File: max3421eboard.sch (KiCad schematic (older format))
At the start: 26 parts, among them J1 USB A, J2 USB MicroB, J3 1x10, J4 1x8, J5 1x8, J6 1x3, J7 Conn_01x04, U1 MAX3421E, U2 LP2985-3.3, U3 STMPS2141STR, Y1 12MHz

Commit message: Added more filtering/bypass and revised layout
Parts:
- added C8: 1u, Capacitors_SMD:C_0805_HandSoldering, symbol Device:C
- added C9: 100n, Capacitors_SMD:C_0805_HandSoldering, symbol Device:C
- added L1: 120 @ 100MHz, Inductors_SMD:L_0805_HandSoldering, symbol Device:L_Core_Ferrite
- U1: symbol MAX3421E:MAX3421E -> max3421eboard-rescue:MAX3421E-MAX3421E
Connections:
- net +3V3: now also C9.1
- net GND: now also C8.2, C9.2
- net VBUS: now also C8.1; no longer J1.1 (VBUS), J7.1 (Pin_1)
- net at C6.1, U1.22 (VBCOMP), U3.1 (OUT): now also J6.3 (Pin_3), J7.1 (Pin_1), L1.1; no longer J2.1 (VBUS), J6.1 (Pin_1)
- net at U3.5 (IN): now also J6.1 (Pin_1); no longer J6.3 (Pin_3)
- new net: J1.1 (VBUS), J2.1 (VBUS), L1.2
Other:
- moved on the sheet: C1, C2, C3, C4, C6, C7, J1, J2, J3, J4, J5, J6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

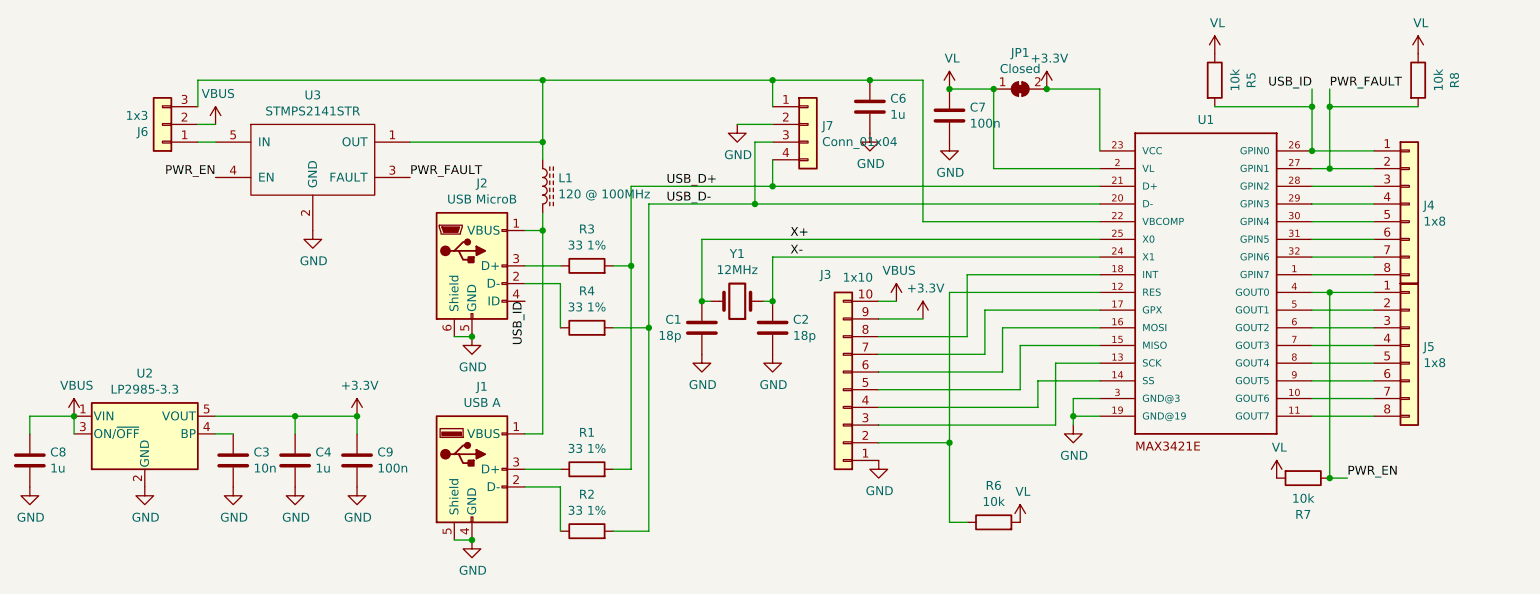
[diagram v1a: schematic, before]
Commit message: Add one more cap and move bypass around even more
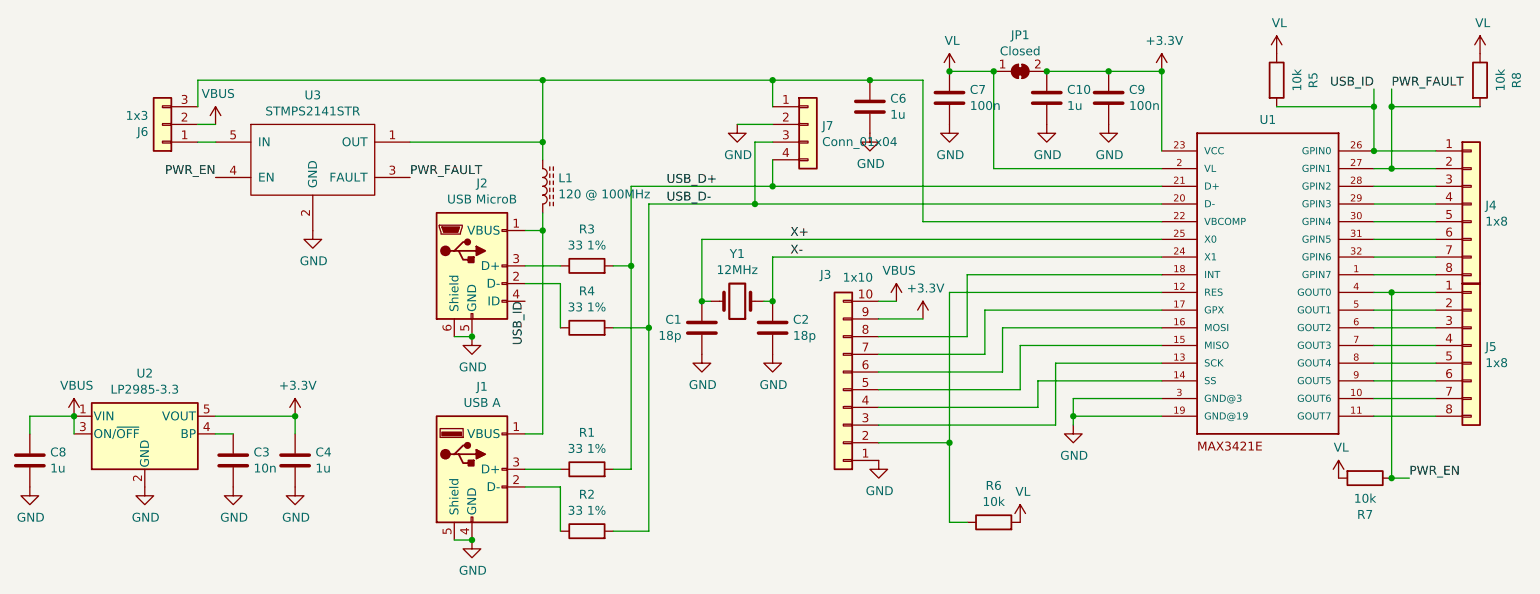
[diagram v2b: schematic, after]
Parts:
- added C10: 1u, Capacitors_SMD:C_0805_HandSoldering, symbol Device:C
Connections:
- net +3V3: now also C10.1
- net GND: now also C10.2
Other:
- moved on the sheet: C7, C9, J4, J5, JP1, R5, R7, R8, U1
